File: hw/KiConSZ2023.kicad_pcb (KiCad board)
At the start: 4 copper layers, 100 x 60 mm, 108 parts, among them J2 Conn_01x06, J3 USB_C_Receptacle_USB2.0, J4 Conn_02x03_Top_Bottom, J5 Conn_02x03_Top_Bottom, J6 BM20B(0.8)-10DS-0.4V, Q10 SK2302AAT, Q11 SK2302AAT, Q12 SK2302AAT, Q13 SK2302AAT, Q14 SK2302AAT, Q15 SK2302AAT, Q16 SK2302AAT, Q17 SK2301AAT, Q2 SK2302AAT, Q3 SK2302AAT, Q4 SK2302AAT, Q5 SK2302AAT, Q6 SK2302AAT, Q7 SK2302AAT, Q8 SK2302AAT, Q9 SK2302AAT, SW2 SKRPACE010, SW3 SKRPACE010, SW4 SW_SPDT, U2 N32L406RBL7, U3 PUSB3FR4, U4 SY8088IAAC, U5 ME2118C33M5G

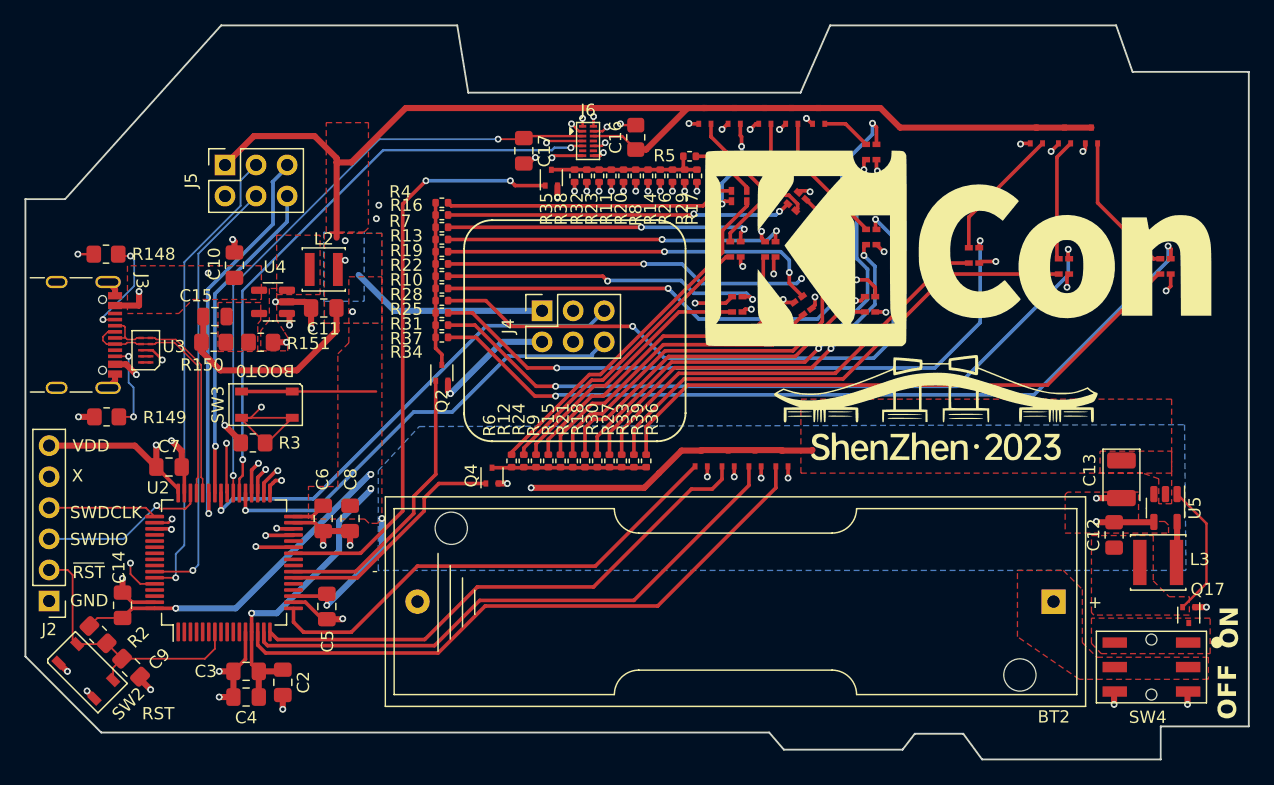
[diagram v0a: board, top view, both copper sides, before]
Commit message: rotated XL-1615 RGB LED
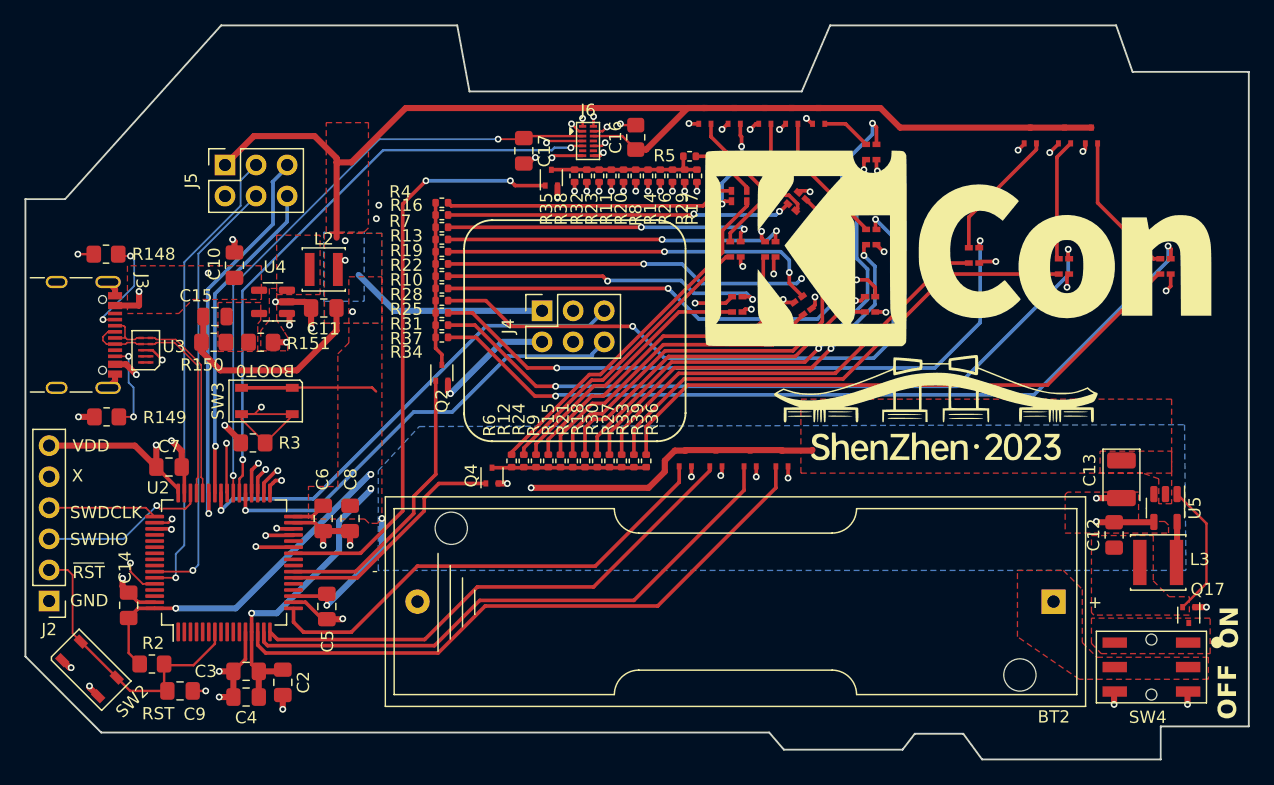
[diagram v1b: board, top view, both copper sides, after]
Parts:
- moved R2 5.01 mm to (60.6, 136.0), turned to 0 degrees
- moved C9 4.43 mm to (62.9, 138.2), turned to 0 degrees
- moved Q8 1.30 mm to (104.2, 119.2)
- moved Q9 1.00 mm to (106.7, 119.2)
- moved C14 0.50 mm to (58.7, 131.2)
- moved Q14 0.50 mm to (132.4, 92.8)
- moved Q11 0.40 mm to (109.5, 119.2)
- moved SW2 0.36 mm to (55.5, 136.4)
- moved SW3 0.30 mm to (70.0, 114.5)
- turned D10 to 180 degrees
- turned D11 to 180 degrees
- turned D12 to 180 degrees
- turned D13 to 180 degrees
- turned D2 to -90 degrees
- turned D3 to 180 degrees
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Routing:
- net /HighSide_Row_4: track 43.7 -> 42.3 mm
- net VDDA: track 266.9 -> 268.2 mm
- net /MCU/~{RST}: track 23.5 -> 24.8 mm
- net /HighSide_Row_10: track 87.8 -> 87.2 mm
- net Net-(D4-A): track 19.0 -> 18.4 mm
- net /HighSide_Row_3: track 39.9 -> 39.4 mm
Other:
- outline, holes or cut-outs redrawn

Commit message: changed to use N-MOS as Reverse Battery Protection Circuits
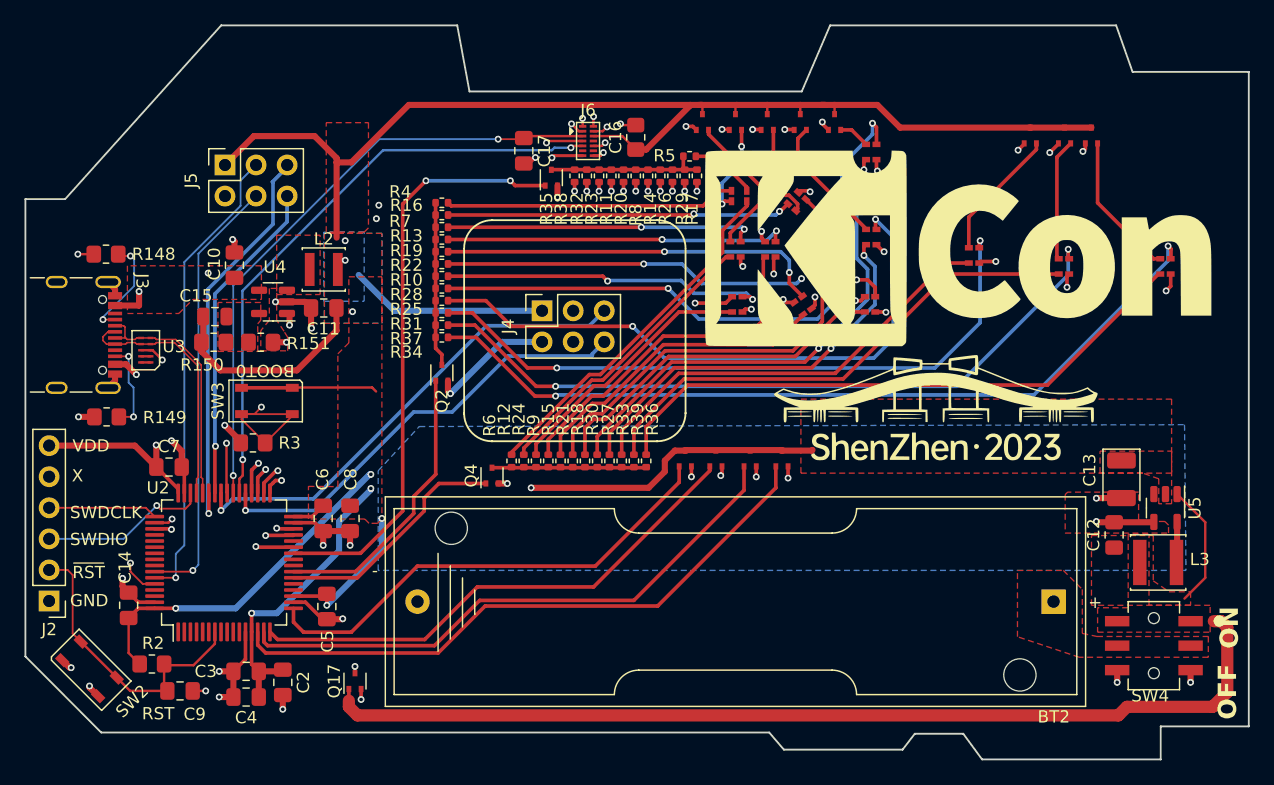
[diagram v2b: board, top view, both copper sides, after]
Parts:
- Q17: value SK2301AAT -> SK2302AAT
- moved Q17 68.4 mm to (77.2, 137.4), turned to 90 degrees
- moved SW4 1.76 mm to (142.5, 134.5)
- moved Q13 1.39 mm to (116.4, 91.7)
- moved Q12 0.86 mm to (113.6, 91.7)
- moved Q10 0.54 mm to (110.9, 91.7)
- moved Q7 0.54 mm to (105.6, 91.7)
- moved Q6 0.51 mm to (108.3, 91.7)
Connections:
- BT2 pad 2: GND -> /Power/Battery-
- Q17 pad 1: GND -> /Power/Battery_In
- Q17 pad 2: /Power/Battery_In -> GND
- Q17 pad 3: /Power/Battery_SW -> /Power/Battery-
- SW4 pad 1: /Power/Battery_SW -> /Power/Battery_In
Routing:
- net /Power/Battery_In: track 11.0 -> 91.1 mm
- net /Power/Battery-: track 0.00 -> 8.39 mm, vias 0 -> 1
- net VDDA: track 268.2 -> 271.8 mm
- net Net-(D10-A): track 4.07 -> 2.56 mm
- net /HighSide_Row_7: track 58.9 -> 60.1 mm
- net Net-(D6-A): track 8.24 -> 7.66 mm
- net Net-(D2-A): track 8.16 -> 7.61 mm
- removed copper zone on F.Cu, net /Power/Battery_SW

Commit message: updated track
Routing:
- net /LED Row/LowSide_Input_Source_B: track 12.6 -> 21.0 mm
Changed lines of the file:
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@@
   (segment (start 93.265 95.59) (end 95.15 95.59) (width 0.3) (layer "F.Cu") (net 46))
   (segment (start 93.25 95.605) (end 93.265 95.59) (width 0.3) (layer "F.Cu") (net 46))
-  (segment (start 88.4 119.955) (end 100.955 119.955) (width 0.3) (layer "F.Cu") (net 47))
-  (segment (start 100.955 119.955) (end 101 119.91) (width 0.3) (layer "F.Cu") (net 47))
+  (segment (start 90 120.6) (end 91 120.6) (width 0.3) (layer "F.Cu") (net 47))
+  (segment (start 88.755 119.955) (end 89.4 120.6) (width 0.3) (layer "F.Cu") (net 47))
+  (segment (start 100 119.91) (end 100 120.6) (width 0.2) (layer "F.Cu") (net 47))
+  (segment (start 99 119.91) (end 99 120.6) (width 0.2) (layer "F.Cu") (net 47))
+  (segment (start 98 119.91) (end 98 120.6) (width 0.2) (layer "F.Cu") (net 47))
+  (segment (start 90 119.91) (end 90 120.6) (width 0.2) (layer "F.Cu") (net 47))
+  (segment (start 91 120.6) (end 92.1 120.6) (width 0.3) (layer "F.Cu") (net 47))
+  (segment (start 100.6 120.6) (end 101 120.2) (width 0.3) (layer "F.Cu") (net 47))
+  (segment (start 96 119.91) (end 96 120.6) (width 0.2) (layer "F.Cu") (net 47))
+  (segment (start 101 120.2) (end 101 119.91) (width 0.3) (layer "F.Cu") (net 47))
+  (segment (start 97 120.6) (end 98 120.6) (width 0.3) (layer "F.Cu") (net 47))
+  (segment (start 88.4 119.955) (end 88.755 119.955) (width 0.3) (layer "F.Cu") (net 47))
+  (segment (start 89.4 120.6) (end 90 120.6) (width 0.3) (layer "F.Cu") (net 47))
+  (segment (start 92.1 120.6) (end 93 120.6) (width 0.3) (layer "F.Cu") (net 47))
+  (segment (start 99 120.6) (end 100 120.6) (width 0.3) (layer "F.Cu") (net 47))
+  (segment (start 97 119.91) (end 97 120.6) (width 0.2) (layer "F.Cu") (net 47))
+  (segment (start 96 120.6) (end 97 120.6) (width 0.3) (layer "F.Cu") (net 47))
+  (segment (start 100 120.6) (end 100.6 120.6) (width 0.3) (layer "F.Cu") (net 47))
+  (segment (start 93 119.91) (end 93 120.6) (width 0.2) (layer "F.Cu") (net 47))
+  (segment (start 98 120.6) (end 99 120.6) (width 0.3) (layer "F.Cu") (net 47))
+  (segment (start 91 119.91) (end 91 120.6) (width 0.2) (layer "F.Cu") (net 47))
+  (segment (start 94 120.6) (end 94.9 120.6) (width 0.3) (layer "F.Cu") (net 47))
+  (segment (start 92 119.91) (end 92 120.5) (width 0.2) (layer "F.Cu") (net 47))
+  (segment (start 95 120.5) (end 94.9 120.6) (width 0.2) (layer "F.Cu") (net 47))
+  (segment (start 94.9 120.6) (end 96 120.6) (width 0.3) (layer "F.Cu") (net 47))
+  (segment (start 94 119.91) (end 94 120.6) (width 0.2) (layer "F.Cu") (net 47))
+  (segment (start 93 120.6) (end 94 120.6) (width 0.3) (layer "F.Cu") (net 47))
+  (segment (start 95 119.91) (end 95 120.5) (width 0.2) (layer "F.Cu") (net 47))
+  (segment (start 92 120.5) (end 92.1 120.6) (width 0.2) (layer "F.Cu") (net 47))
   (segment (start 67.925 115.575) (end 68.975 115.575) (width 0.15) (layer "F.Cu") (net 48))
   (segment (start 67.925 115.575) (end 72.075 115.575) (width 0.15) (layer "F.Cu") (net 48))

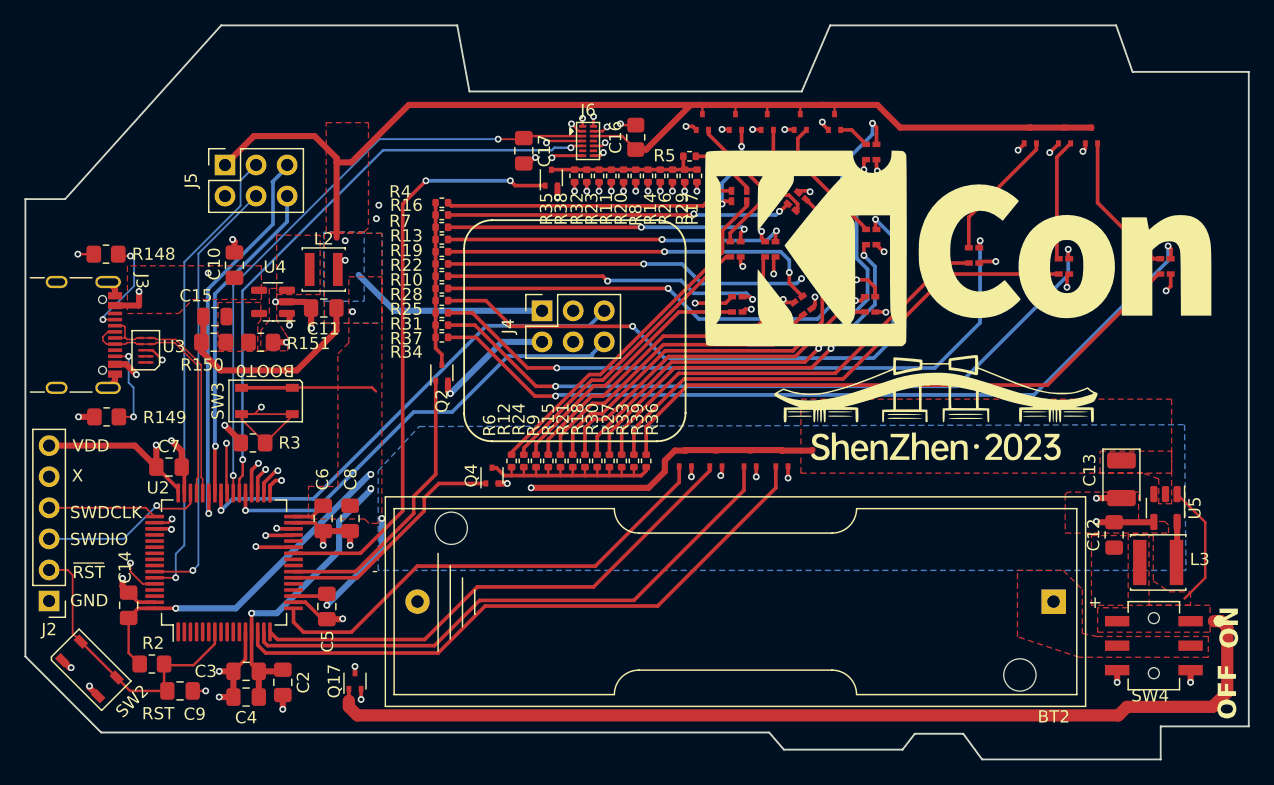
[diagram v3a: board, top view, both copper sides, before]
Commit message: added two smt marks
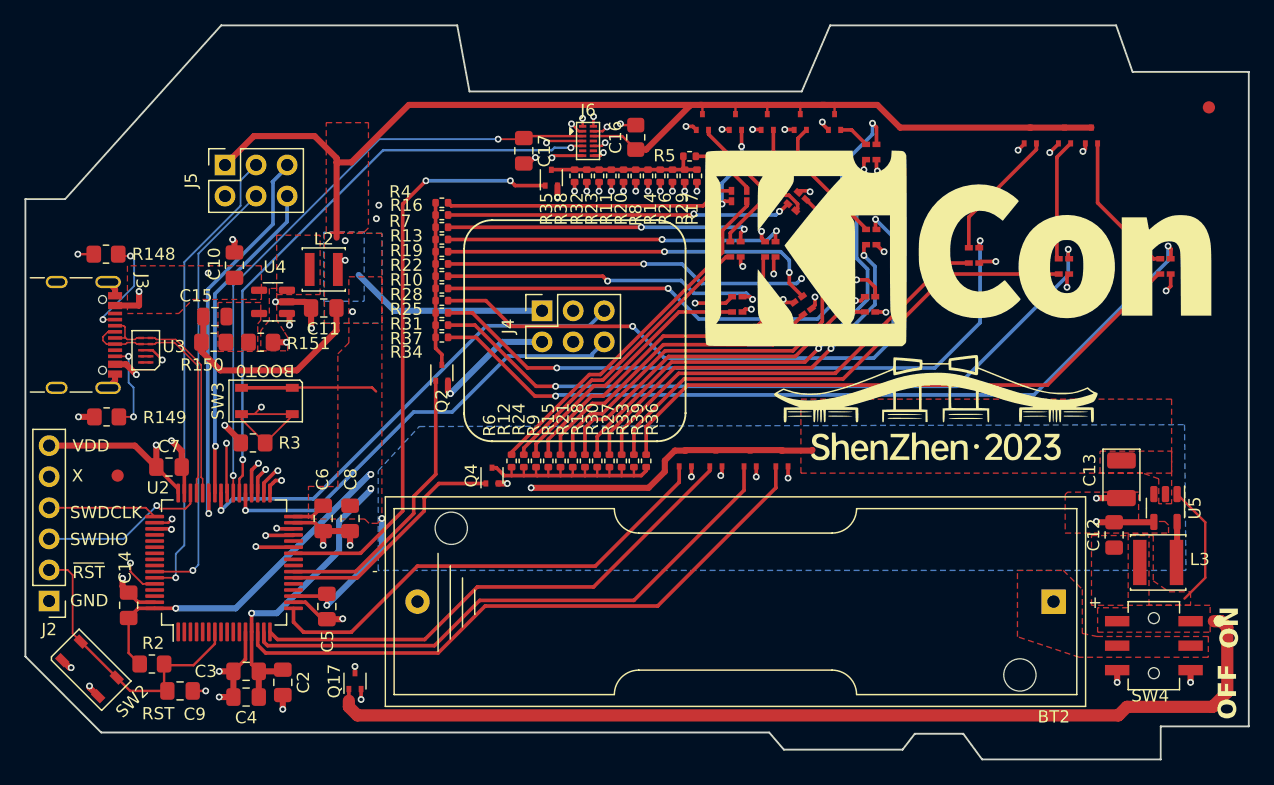
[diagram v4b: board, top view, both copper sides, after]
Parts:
- added REF**: SMT_Mark, IotPi_TestPoints_Marks:SMT_Mark, F.Cu at (147.0, 90.5)
- added REF**: SMT_Mark, IotPi_TestPoints_Marks:SMT_Mark, F.Cu at (57.8, 120.6)
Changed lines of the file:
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@@
       (stroke (width 0) (type solid)) (fill solid) (layer "F.SilkS"))
+  )
+  (footprint "IotPi_TestPoints_Marks:SMT_Mark" (layer "F.Cu")
+    (at 147 90.5)
+    (attr board_only exclude_from_bom)
+    (fp_text reference "REF**" (at 0 -0.5 unlocked) (layer "F.SilkS") hide
+        (effects (font (size 1 1) (thickness 0.1)))
+    )
+    (fp_text value "SMT_Mark" (at 0 1 unlocked) (layer "F.Fab")
+        (effects (font (size 1 1) (thickness 0.15)))
+    )
+    (fp_text user "${REFERENCE}" (at 0 2.5 unlocked) (layer "F.Fab")
+        (effects (font (size 1 1) (thickness 0.15)))
+    )
+    (pad "1" smd circle (at 0 0) (size 1 1) (layers "F.Cu" "F.Paste" "F.Mask")
+      (solder_mask_margin 0.5))
   )
   (footprint "Connector_PinSocket_2.54mm:PinSocket_2x03_P2.54mm_Vertical" (layer "F.Cu")
@@
     )
   )
+  (footprint "IotPi_TestPoints_Marks:SMT_Mark" (layer "F.Cu")
+    (at 57.8 120.6)
+    (attr board_only exclude_from_bom)
+    (fp_text reference "REF**" (at 0 -0.5 unlocked) (layer "F.SilkS") hide
+        (effects (font (size 1 1) (thickness 0.1)))
+    )
+    (fp_text value "SMT_Mark" (at 0 1 unlocked) (layer "F.Fab")
+        (effects (font (size 1 1) (thickness 0.15)))
+    )
+    (fp_text user "${REFERENCE}" (at 0 2.5 unlocked) (layer "F.Fab")
+        (effects (font (size 1 1) (thickness 0.15)))
+    )
+    (pad "1" smd circle (at 0 0) (size 1 1) (layers "F.Cu" "F.Paste" "F.Mask")
+      (solder_mask_margin 0.5))
+  )
   (footprint "Capacitor_SMD:C_0805_2012Metric_Pad1.18x1.45mm_HandSolder" (layer "F.Cu")
